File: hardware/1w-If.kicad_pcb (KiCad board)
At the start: 2 copper layers, 68 x 85 mm, 50 parts, among them U1 WT32-ETH01, U2 TCA9548APWR, U3 DS2484R, U4 DS2484R, U5 DS2484R, U6 DS2484R, X1 PowerSupply, X2 Debug Terminal, X3 Ext LED Terminal, X4 1-Wire Ch1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

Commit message: C1-C4: Fix polarity | R1+R3: Adapt for 20mA external LEDs
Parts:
- D1: value LED Power -> LED Power 5mA
- D2: value LED Status -> LED Status 5mA
- R1, R3: value 100 -> 22
- turned C1 to 180 degrees
- turned C2 to 180 degrees
- turned C3 to -90 degrees
- turned C4 to 90 degrees
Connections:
- C1 pad 1: GND -> +5V
- C1 pad 2: +5V -> GND
- C2 pad 1: GND -> +5V
- C2 pad 2: +5V -> GND
- C3 pad 1: GND -> /WT32_ETH01_EN
- C3 pad 2: /WT32_ETH01_EN -> GND
- C4 pad 1: GND -> +3.3V
- C4 pad 2: +3.3V -> GND
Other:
- board text added: "v 1.1"
- board text removed: "v 1.0"

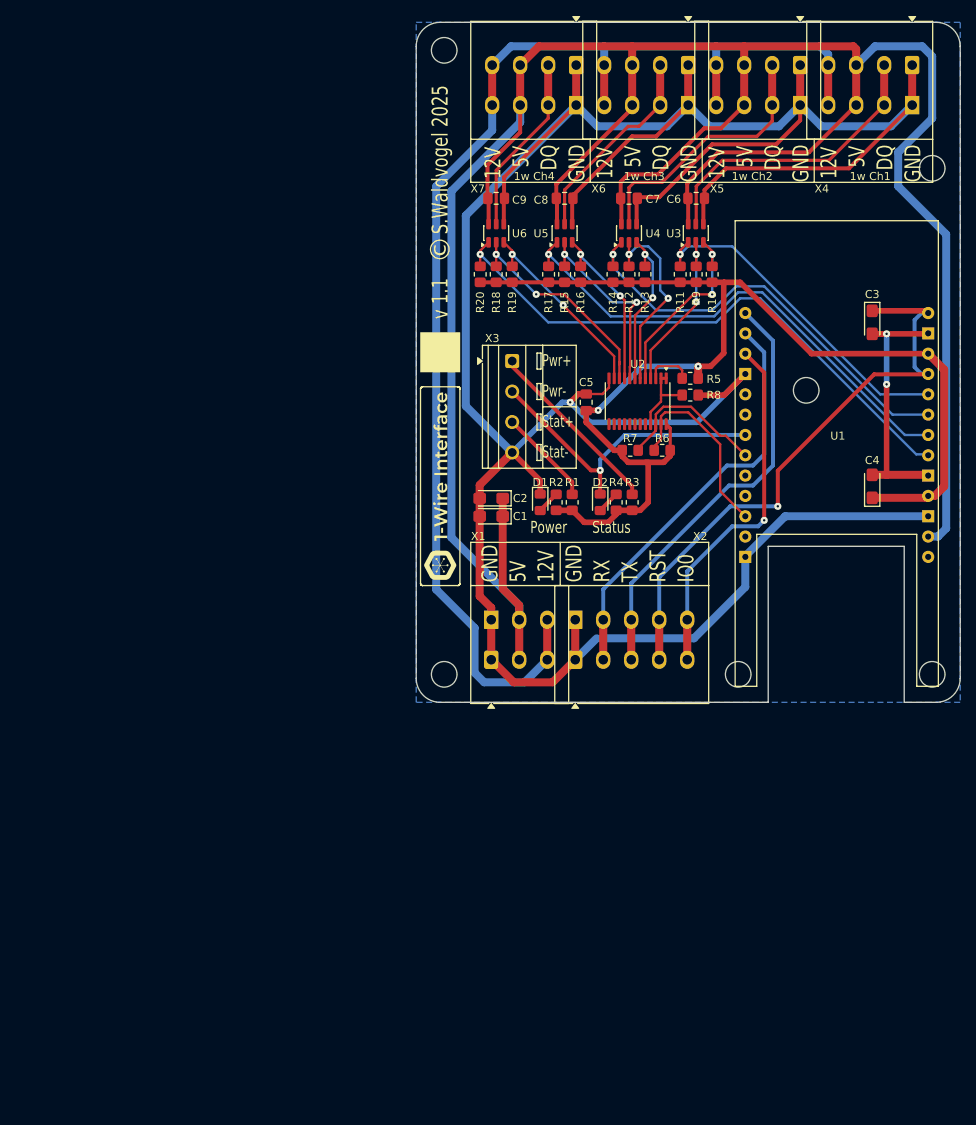
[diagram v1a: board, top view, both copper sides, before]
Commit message: - Too bright LEDs: R1-R4 changed to 1kOhm - Swapped ext. LED connector silk layer description
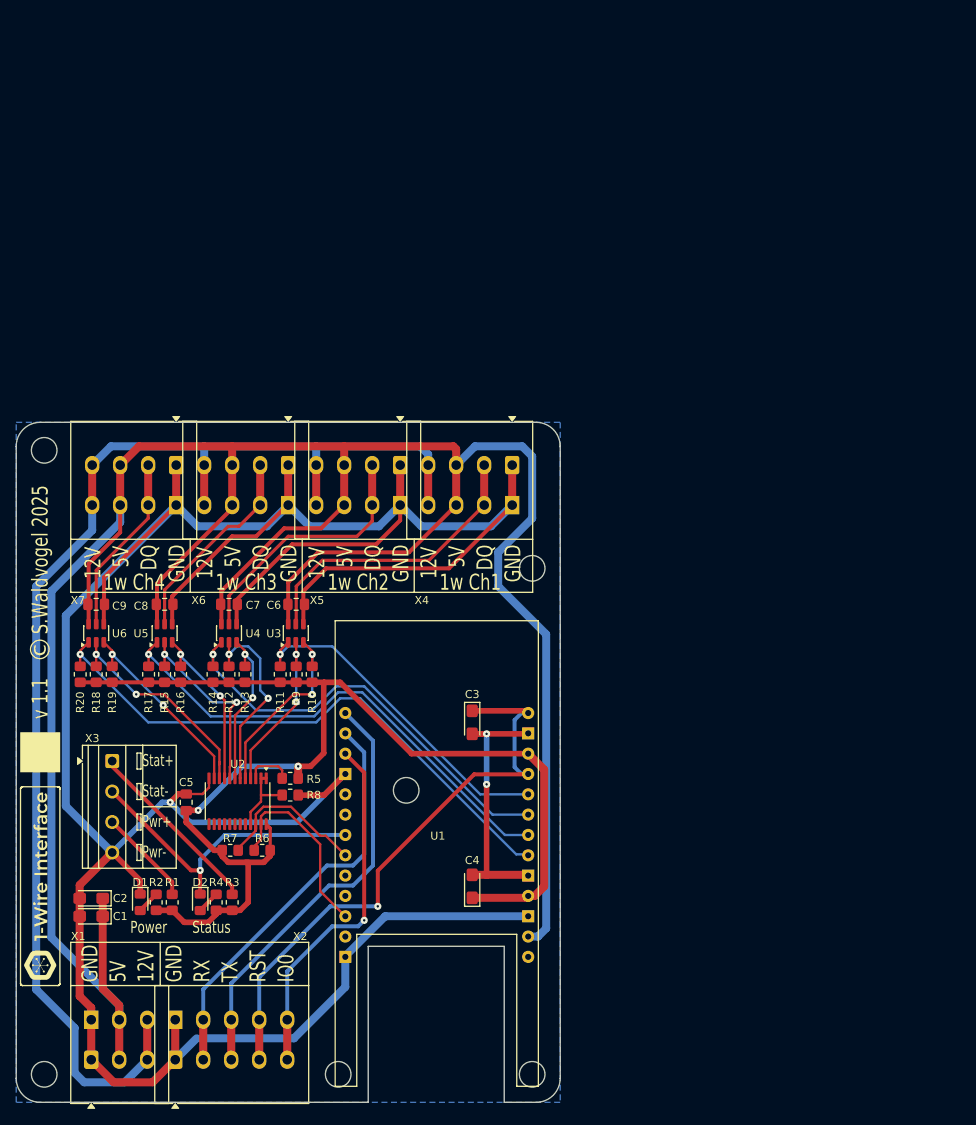
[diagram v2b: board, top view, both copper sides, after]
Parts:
- R1, R3: value 22 -> 1k
- R2, R4: value 100 -> 1k
- moved C6 71.2 mm to (109.0, 113.8)
- moved C7 71.2 mm to (100.6, 113.8)
- moved C8 71.2 mm to (92.5, 113.8)
- moved C9 71.2 mm to (84.0, 113.8)
- moved U2 70.7 mm to (101.7, 138.4)
- moved R15 70.7 mm to (92.5, 122.5)
- moved R16 70.7 mm to (94.5, 122.5)
- moved R17 70.7 mm to (90.5, 122.5)
- moved U5 70.7 mm to (92.5, 117.4)
- moved X1 70.7 mm to (83.4, 170.7)
- moved X2 70.7 mm to (93.9, 170.7)
- moved C1 70.7 mm to (83.4, 152.8)
- moved C2 70.7 mm to (83.4, 150.5)
- moved C3 70.7 mm to (131.0, 128.5)
- moved C4 70.7 mm to (131.0, 149.0)
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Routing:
- net +5V: track 332.0 -> 328.7 mm
- net GND: track 415.8 -> 414.7 mm
- net /OW_Ch2: track 32.9 -> 32.3 mm
